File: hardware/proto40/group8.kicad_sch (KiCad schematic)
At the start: 36 parts, among them U1101 TMUX1308, U1102 74HC165

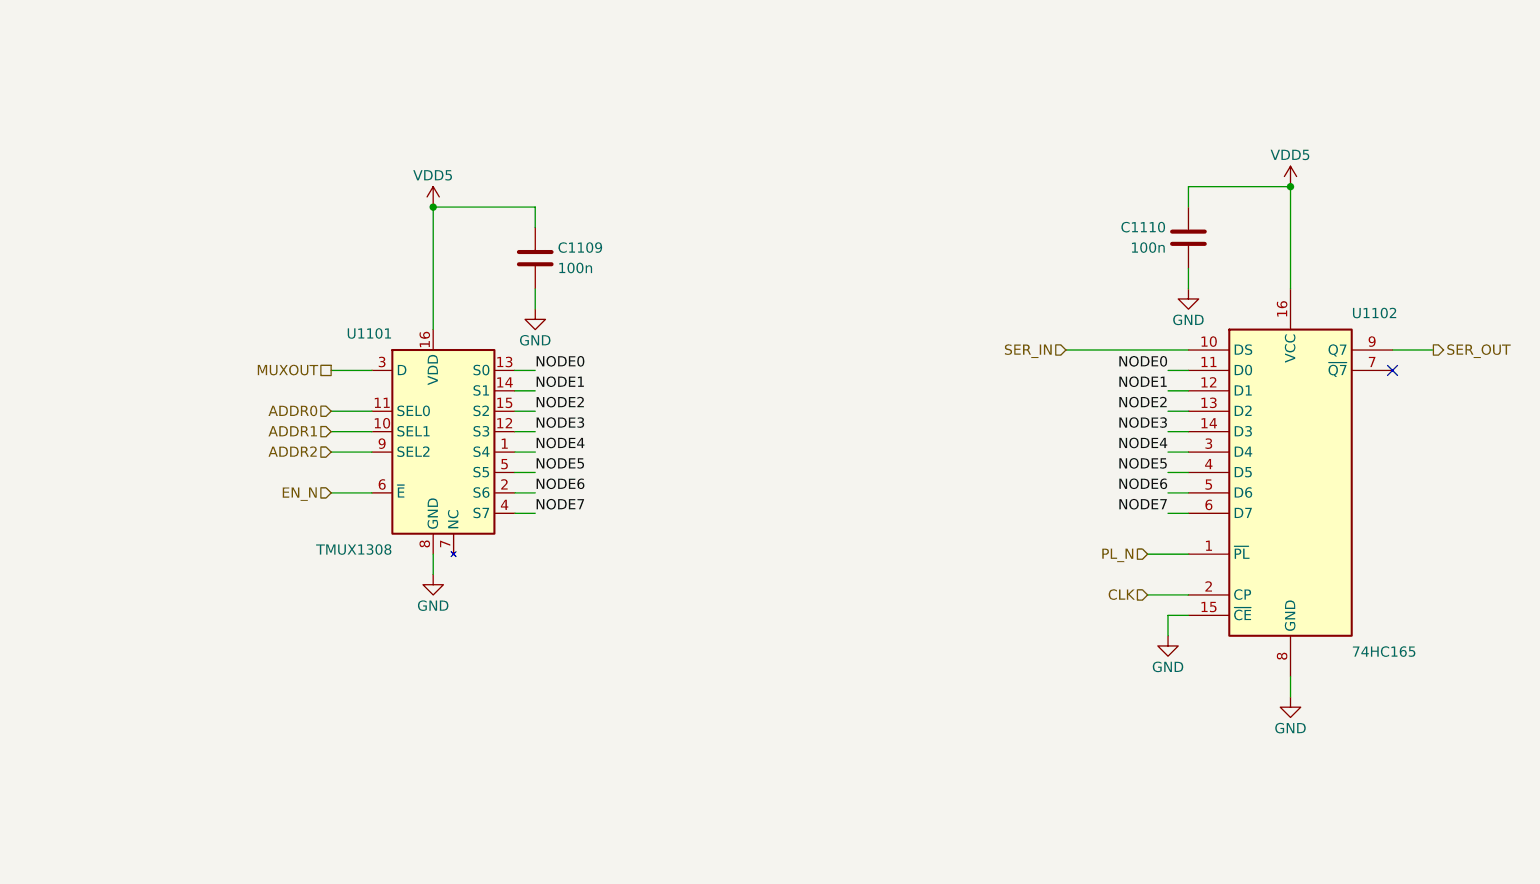
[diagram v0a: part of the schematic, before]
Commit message: Resolve Proto40 house-style review findings
- Fixture ID lines: TVS at the connector plus series R on SDA/SCL/WP/A0/PRESENT_N;
  ID_VCC limited by 100 ohm 1206 (D14). PRESENT_N pull-up moved to MCU side.
- Shunt clamp ballast R104 is 6.8 ohm 2512, BCP53 copper note (D15).
- MPN/Manufacturer on every part (generic Yageo/Samsung passives), LCSC TBD.
- Test points on the '595 outputs and chain in/out; pull-downs on SCK/RCLK.
- Root sheet: CTRL/SENSE chains and ID lines drawn as wires; ASCII-only text.
- layoutcheck: non-ASCII, title length, text/text gap, text/wire clearance,
  NC flag on wired pin; wider char estimate. CI ERC runs --severity-all.
- Netclass patterns tightened for STIM/MUX and SPI nets.

Co-Authored-By: Claude Opus 5.5 (1M context) <noreply@anthropic.com>
Claude-Session: https://claude.ai/code/session_013SDanWEFU4wFXEYfZ6C9GH
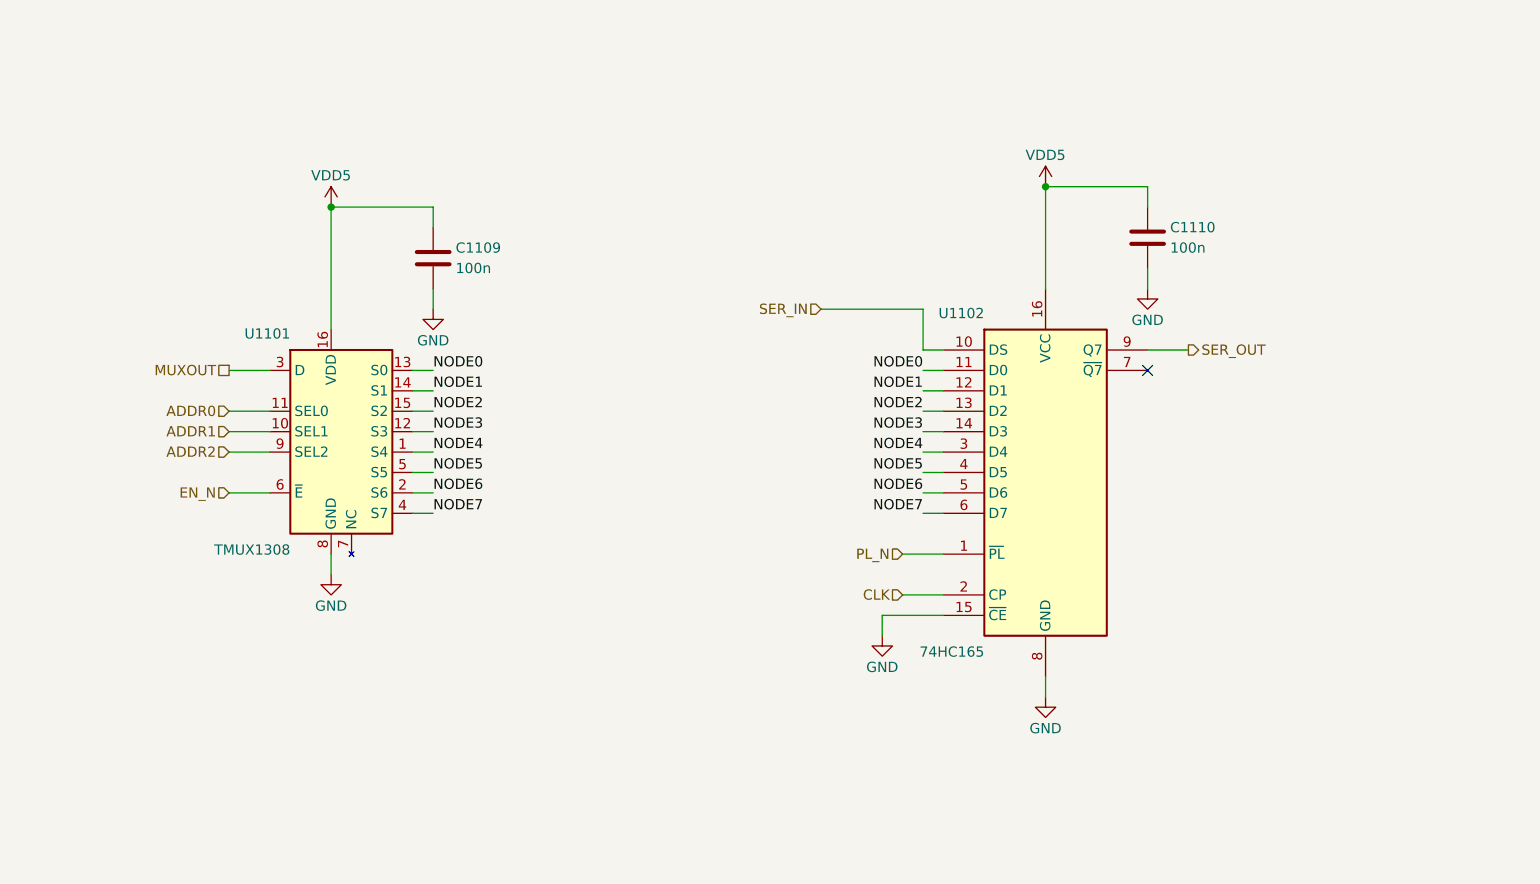
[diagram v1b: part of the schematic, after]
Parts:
- C1101, C1102, C1103, C1104, C1105, C1106, C1107, C1108: LCSC (none) -> TBD; MPN (none) -> CL10C101JB8NNNC; Manufacturer (none) -> Samsung Electro-Mechanics
- C1109, C1110: LCSC (none) -> TBD; MPN (none) -> CL10B104KB8NNNC; Manufacturer (none) -> Samsung Electro-Mechanics
- D1101, D1102, D1103, D1104, D1105, D1106, D1107, D1108, U1102: LCSC (none) -> TBD
- R1101, R1103, R1105, R1107, R1109, R1111, R1113, R1115: LCSC (none) -> TBD; MPN 1206 4.7 kΩ 1 % 0.25 W -> RC1206FR-074K7L; Manufacturer (none) -> Yageo; Note Rs, fault-rated, see sim -> Rs, 0.25 W, fault-rated, see sim
- R1102, R1104, R1106, R1108, R1110, R1112, R1114, R1116: LCSC (none) -> TBD; MPN 0603 680 kΩ 1 % -> RC0603FR-07680KL; Manufacturer (none) -> Yageo
- U1101: LCSC (none) -> TBD; MPN (none) -> TMUX1308PWR; Manufacturer (none) -> Texas Instruments
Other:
- title: Proto40 – 8-channel group -> Proto40 - 8-channel group
- moved on the sheet: C1109, C1110, U1101, U1102
